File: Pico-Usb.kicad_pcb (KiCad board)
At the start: 2 copper layers, 25 x 60 mm, 40 parts, among them J1 USB_A, J3 MEM2067-02-180-00-A_REVB, J4 10133475-10001LF, SW4 A6H-4101, U1 RP2040, U2 W25Q128JVS, U3 MAX40200AUK, U4 MAX40200AUK, U5 AP2112K-3.3, U6 TS3USB221ARSER, Y2 ABM3B-12.000MHZ-10-1-U-T

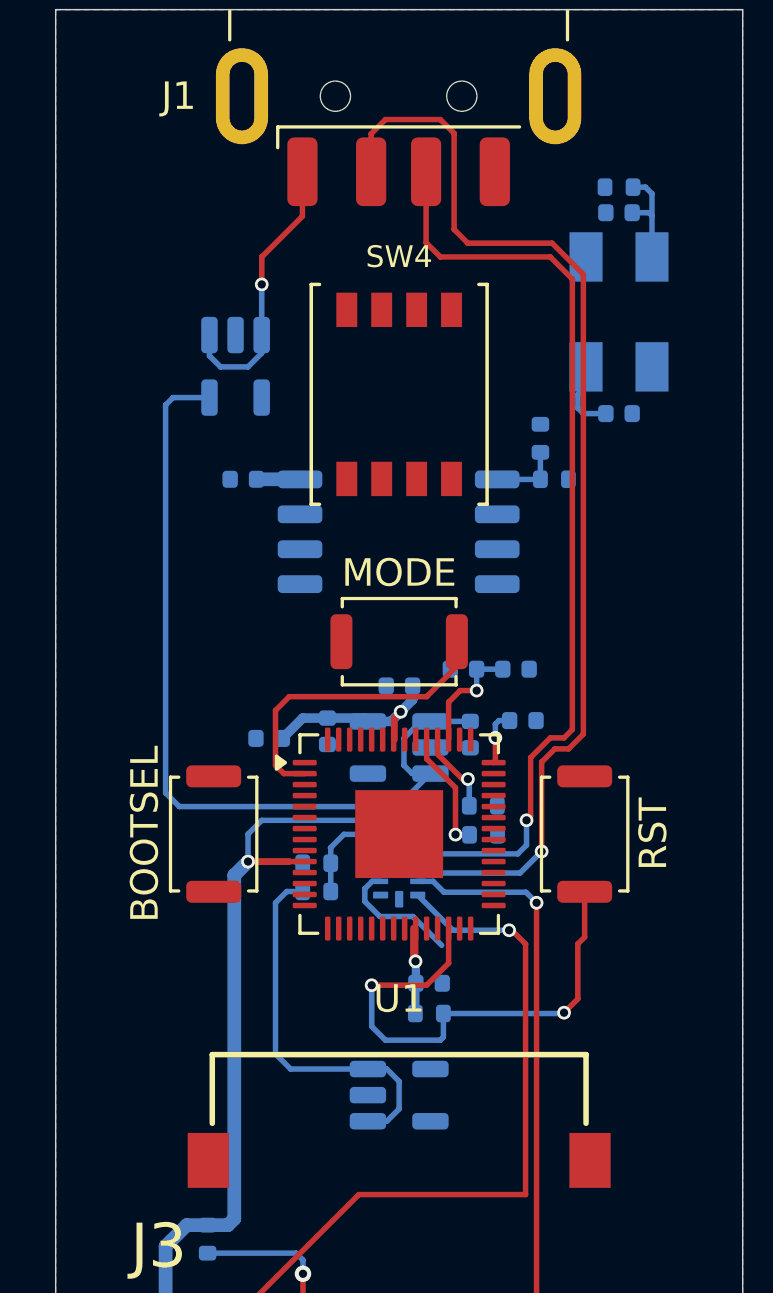
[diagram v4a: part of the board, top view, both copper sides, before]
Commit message: Cambie dimensiones de pistas
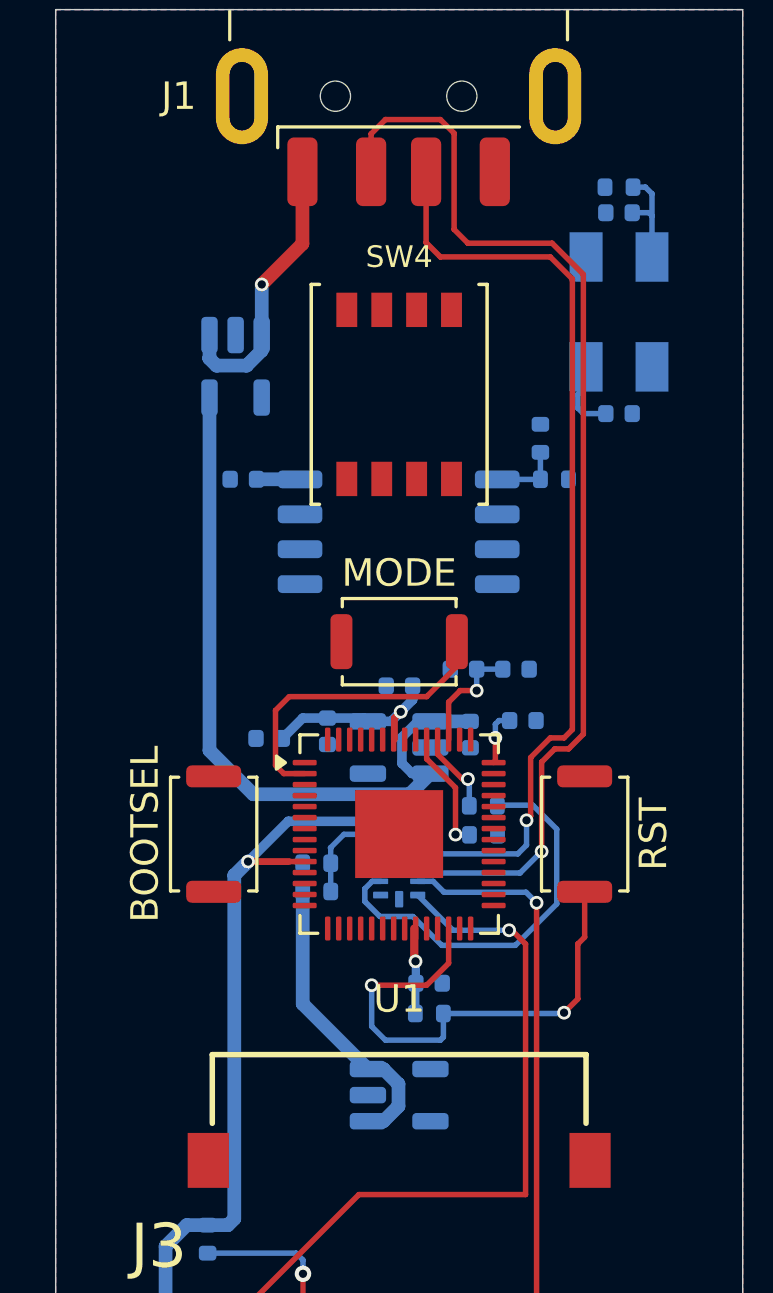
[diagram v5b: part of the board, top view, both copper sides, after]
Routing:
- net /MCU_D-: track 4.61 -> 14.7 mm
- net /5V_Secure: track 30.9 -> 26.7 mm
- net VBUS_A: track 13.9 -> 10.9 mm
- net /3.3V: track 58.0 -> 57.2 mm
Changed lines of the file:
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@@
+	)
+	(segment
+		(start 136.765379 99.535379)
+		(end 133.464621 99.535379)
+		(width 0.35)
+		(layer "B.Cu")
+		(net "/3.3V")
 	)
 	(segment
@@
 		(end 137.20652 95.9)
 		(width 0.35)
-		(layer "B.Cu")
-		(net "/3.3V")
-	)
-	(segment
-		(start 137 99.5)
-		(end 132.5 99.5)
-		(width 0.2)
 		(layer "B.Cu")
 		(net "/3.3V")
@@
 	)
 	(segment
-		(start 137.5 100)
-		(end 137 99.5)
-		(width 0.2)
-		(layer "B.Cu")
-		(net "/3.3V")
-	)
-	(segment
 		(start 142.57 116.99)
 		(end 141.705444 116.99)
@@
 	)
 	(segment
-		(start 137.5 100.57)
-		(end 137.5 100)
-		(width 0.2)
-		(layer "B.Cu")
-		(net "/3.3V")
-	)
-	(segment
 		(start 129.77 114.23)
 		(end 130.53 114.23)
@@
 	)
 	(segment
+		(start 137.5 100.27)
+		(end 136.765379 99.535379)
+		(width 0.35)
+		(layer "B.Cu")
+		(net "/3.3V")
+	)
+	(segment
 		(start 131.8 117.19)
 		(end 129.19 117.19)
 		(width 0.5)
-		(layer "B.Cu")
-		(net "/3.3V")
-	)
-	(segment
-		(start 132.5 99.5)
-		(end 132 100)
-		(width 0.2)
 		(layer "B.Cu")
 		(net "/3.3V")
@@
 	)
 	(segment
-		(start 132 100)
-		(end 132 101)
-		(width 0.2)
-		(layer "B.Cu")
-		(net "/3.3V")
-	)
-	(segment
 		(start 131.5 114)
 		(end 131.5 101.5)
 		(width 0.5)
+		(layer "B.Cu")
+		(net "/3.3V")
+	)
+	(segment
+		(start 133.464621 99.535379)
+		(end 132 101)
+		(width 0.35)
+		(layer "B.Cu")
+		(net "/3.3V")
+	)
+	(segment
+		(start 137.5 100.57)
+		(end 137.5 100.27)
+		(width 0.35)
 		(layer "B.Cu")
 		(net "/3.3V")
@@
 	)
 	(segment
-		(start 132.5 80)
-		(end 132.5 79)
-		(width 0.2)
+		(start 133.98 75.9)
+		(end 133.98 78.52)
+		(width 0.5)
 		(layer "F.Cu")
 		(net "Net-(J1-VBUS)")
 	)
 	(segment
-		(start 132.5 79)
-		(end 133.98 77.52)
-		(width 0.2)
-		(layer "F.Cu")
-		(net "Net-(J1-VBUS)")
-	)
-	(segment
-		(start 133.98 77.52)
-		(end 133.98 75.9)
-		(width 0.2)
+		(start 133.98 78.52)
+		(end 132.5 80)
+		(width 0.5)
 		(layer "F.Cu")
 		(net "Net-(J1-VBUS)")
@@
 	(segment
 		(start 130.5975 81.8425)
-		(end 130.5975 82.5975)
-		(width 0.2)
+		(end 130.5975 82.6825)
+		(width 0.5)
 		(layer "B.Cu")
 		(net "Net-(J1-VBUS)")
 	)
 	(segment
-		(start 130.5975 82.5975)
-		(end 131 83)
-		(width 0.2)
+		(start 130.855 82.955)
+		(end 131.950184 82.955)
+		(width 0.5)
+		(layer "B.Cu")
+		(net "Net-(J1-VBUS)")
+	)
+	(segment
+		(start 132.5 81.84)
+		(end 132.4975 81.8425)
+		(width 0.5)
+		(layer "B.Cu")
+		(net "Net-(J1-VBUS)")
+	)
+	(segment
+		(start 130.59 82.69)
+		(end 130.855 82.955)
+		(width 0.5)
+		(layer "B.Cu")
+		(net "Net-(J1-VBUS)")
+	)
+	(segment
+		(start 130.5975 82.6825)
+		(end 130.59 82.69)
+		(width 0.5)
 		(layer "B.Cu")
 		(net "Net-(J1-VBUS)")
@@
 	)
 	(segment
-		(start 132.4975 82.5025)
+		(start 132.5 80)
+		(end 132.5 81.84)
+		(width 0.5)
+		(layer "B.Cu")
+		(net "Net-(J1-VBUS)")
+	)
+	(segment
+		(start 132.4975 82.407684)
 		(end 132.4975 81.8425)
-		(width 0.2)
+		(width 0.5)
 		(layer "B.Cu")
 		(net "Net-(J1-VBUS)")
 	)
 	(segment
-		(start 132 83)
-		(end 132.4975 82.5025)
-		(width 0.2)
-		(layer "B.Cu")
-		(net "Net-(J1-VBUS)")
-	)
-	(segment
-		(start 132.4975 81.8425)
-		(end 132.4975 80.0025)
-		(width 0.2)
-		(layer "B.Cu")
-		(net "Net-(J1-VBUS)")
-	)
-	(segment
-		(start 131 83)
-		(end 132 83)
-		(width 0.2)
+		(start 131.950184 82.955)
+		(end 132.4975 82.407684)
+		(width 0.5)
 		(layer "B.Cu")
 		(net "Net-(J1-VBUS)")
@@
 	)
 	(segment
-		(start 133 108)
-		(end 133 102.5)
-		(width 0.2)
+		(start 136.927684 110.45)
+		(end 136.3625 110.45)
+		(width 0.5)
 		(layer "B.Cu")
 		(net "VBUS_A")
 	)
 	(segment
-		(start 137.05 108.55)
+		(start 133.99 106.1775)
 		(end 136.3625 108.55)
-		(width 0.2)
+		(width 0.5)
 		(layer "B.Cu")
 		(net "VBUS_A")
 	)
 	(segment
-		(start 137.5 110)
-		(end 137.5 109)
-		(width 0.2)
+		(start 136.927684 108.55)
+		(end 137.475 109.097316)
+		(width 0.5)
 		(layer "B.Cu")
 		(net "VBUS_A")
 	)
 	(segment
-		(start 137.05 110.45)
-		(end 137.5 110)
-		(width 0.2)
+		(start 136.3625 108.55)
+		(end 136.927684 108.55)
+		(width 0.5)
 		(layer "B.Cu")
 		(net "VBUS_A")
 	)
 	(segment
-		(start 133.410001 102.089999)
-		(end 133.99 102.089999)
-		(width 0.2)
+		(start 137.475 109.097316)
+		(end 137.475 109.902684)
+		(width 0.5)
 		(layer "B.Cu")
 		(net "VBUS_A")
 	)
 	(segment
-		(start 136.3625 110.45)
-		(end 137.05 110.45)
-		(width 0.2)
+		(start 137.475 109.902684)
+		(end 136.927684 110.45)
+		(width 0.5)
 		(layer "B.Cu")
 		(net "VBUS_A")
 	)
 	(segment
-		(start 133 102.5)
-		(end 133.410001 102.089999)
-		(width 0.2)
-		(layer "B.Cu")
-		(net "VBUS_A")
-	)
-	(segment
-		(start 133.55 108.55)
-		(end 133 108)
-		(width 0.2)
-		(layer "B.Cu")
-		(net "VBUS_A")
-	)
-	(segment
-		(start 137.5 109)
-		(end 137.05 108.55)
-		(width 0.2)
-		(layer "B.Cu")
-		(net "VBUS_A")
-	)
-	(segment
-		(start 136.3625 108.55)
-		(end 133.55 108.55)
-		(width 0.2)
+		(start 133.99 102.089999)
+		(end 133.99 106.1775)
+		(width 0.5)
 		(layer "B.Cu")
 		(net "VBUS_A")
@@
 	)
 	(segment
-		(start 129 84.389374)
-		(end 129 98.5)
-		(width 0.2)
+		(start 137.8875 98.55)
+		(end 138.6375 97.8)
+		(width 0.5)
+		(layer "B.Cu")
+		(net "/5V_Secure")
+	)
+	(segment
+		(start 137.6 96.478382)
+		(end 137.6 97.424999)
+		(width 0.35)
+		(layer "B.Cu")
+		(net "/5V_Secure")
+	)
+	(segment
+		(start 138.6375 95.9)
+		(end 138.178382 95.9)
+		(width 0.35)
+		(layer "B.Cu")
+		(net "/5V_Secure")
+	)
+	(segment
+		(start 138.178382 95.9)
+		(end 137.6 96.478382)
+		(width 0.35)
+		(layer "B.Cu")
+		(net "/5V_Secure")
+	)
+	(segment
+		(start 137.6 97.424999)
+		(end 137.975001 97.8)
+		(width 0.35)
 		(layer "B.Cu")
 		(net "/5V_Secure")
@@
 		(start 137.975001 97.8)
 		(end 138.6375 97.8)
-		(width 0.2)
-		(layer "B.Cu")
-		(net "/5V_Secure")
-	)
-	(segment
-		(start 129.271874 84.1175)
-		(end 129 84.389374)
-		(width 0.2)
-		(layer "B.Cu")
-		(net "/5V_Secure")
-	)
-	(segment
-		(start 137.4375 99)
-		(end 138.6375 97.8)
-		(width 0.2)
-		(layer "B.Cu")
-		(net "/5V_Secure")
-	)
-	(segment
-		(start 129.5 99)
-		(end 137.4375 99)
-		(width 0.2)
-		(layer "B.Cu")
-		(net "/5V_Secure")
-	)
-	(segment
-		(start 129 98.5)
-		(end 129.5 99)
-		(width 0.2)
-		(layer "B.Cu")
-		(net "/5V_Secure")
-	)
-	(segment
-		(start 137.675 96.509448)
-		(end 137.675 97.499999)
-		(width 0.2)
-		(layer "B.Cu")
-		(net "/5V_Secure")
-	)
-	(segment
-		(start 137.675 97.499999)
-		(end 137.975001 97.8)
-		(width 0.2)
-		(layer "B.Cu")
-		(net "/5V_Secure")
-	)
-	(segment
-		(start 138.6375 95.9)
-		(end 138.284448 95.9)
-		(width 0.2)
+		(width 0.35)
 		(layer "B.Cu")
 		(net "/5V_Secure")
@@
 		(start 138.6375 95.9)
 		(end 140.09 95.9)
-		(width 0.2)
+		(width 0.5)
 		(layer "B.Cu")
 		(net "/5V_Secure")
 	)
 	(segment
-		(start 138.284448 95.9)
-		(end 137.675 96.509448)
-		(width 0.2)
+		(start 130.5975 84.1175)
+		(end 130.5975 96.9575)
+		(width 0.5)
 		(layer "B.Cu")
 		(net "/5V_Secure")
 	)
 	(segment
-		(start 130.5975 84.1175)
-		(end 129.271874 84.1175)
-		(width 0.2)
+		(start 130.5975 96.9575)
+		(end 132.19 98.55)
+		(width 0.5)
+		(layer "B.Cu")
+		(net "/5V_Secure")
+	)
+	(segment
+		(start 132.19 98.55)
+		(end 137.8875 98.55)
+		(width 0.5)
 		(layer "B.Cu")
 		(net "/5V_Secure")
@@
 	)
 	(segment
+		(start 139.05 104.05)
+		(end 141.727818 104.05)
+		(width 0.2)
+		(layer "B.Cu")
+		(net "/MCU_D-")
+	)
+	(segment
+		(start 143.234204 99.822182)
+		(end 142.362022 98.95)
+		(width 0.2)
+		(layer "B.Cu")
+		(net "/MCU_D-")
+	)
+	(segment
+		(start 141.727818 104.05)
+		(end 143.234204 102.543614)
+		(width 0.2)
+		(layer "B.Cu")
+		(net "/MCU_D-")
+	)
+	(segment
+		(start 141.094667 98.95)
+		(end 141.071735 98.972932)
+		(width 0.2)
+		(layer "B.Cu")
+		(net "/MCU_D-")
+	)
+	(segment
 		(start 136.518176 101.72)
 		(end 136.25 101.988176)
 		(width 0.2)
 		(layer "B.Cu")
+		(net "/MCU_D-")
+	)
+	(segment
+		(start 143.234204 102.543614)
+		(end 143.234204 99.822182)
+		(width 0.2)
+		(layer "B.Cu")
+		(net "/MCU_D-")
+	)
+	(segment
+		(start 142.362022 98.95)
+		(end 141.094667 98.95)
+		(width 0.2)
+		(layer "B.Cu")

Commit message: reconfigure pistas para liberar componentes
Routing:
- net VBUS_A: track 10.9 -> 50.8 mm, vias 0 -> 2
- net Net-(U1-GPIO0): track 11.3 -> 31.5 mm, vias 0 -> 2
- net /MCU_D+: track 0.00 -> 20.0 mm, vias 0 -> 2
- net /3.3V: track 57.2 -> 68.4 mm
- net /QSPI_SS: track 2.55 -> 10.7 mm, vias 0 -> 1
- net /USB_C_D-: track 39.3 -> 44.5 mm, vias 1 -> 2
- net /USB_A_D+: track 34.1 -> 38.4 mm
- net /USB_A_D-: track 40.5 -> 44.6 mm
- net /MCU_D-: track 14.7 -> 16.9 mm
- net /USB_C_D+: track 34.4 -> 36.5 mm, vias 1 -> 2

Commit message: complete el ruteo de la memoria al rp2040
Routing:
- net Net-(U1-XOUT): track 0.00 -> 47.7 mm, vias 0 -> 1
- net Net-(U1-XIN): track 2.73 -> 44.1 mm, vias 0 -> 1
- net Net-(R5-Pad1): track 0.00 -> 25.6 mm, vias 0 -> 5
- net /SPI_RX: track 6.00 -> 26.9 mm, vias 1 -> 2
- net /SPI_CS: track 0.00 -> 15.8 mm, vias 0 -> 2
- net /QSPI_SCLK: track 0.00 -> 13.2 mm, vias 0 -> 3
- net /QSPI_SD3: track 0.00 -> 12.5 mm, vias 0 -> 3
- net /QSPI_SD0: track 0.00 -> 12.5 mm, vias 0 -> 1
- net /QSPI_SD1: track 0.00 -> 12.1 mm, vias 0 -> 1
- net /QSPI_SD2: track 0.00 -> 10.9 mm, vias 0 -> 1
- net VBUS_A: track 50.8 -> 60.3 mm
- net /QSPI_SS: track 10.7 -> 19.5 mm
- net GNDREF: track 0.00 -> 7.23 mm
- net /3.3V: track 68.4 -> 71.5 mm, vias 5 -> 6
- net Net-(U1-RUN): track 18.7 -> 18.2 mm

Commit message: Termine el ruteo
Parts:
- renumbered SW4 to CFG
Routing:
- net /SWD-1: track 0.00 -> 39.0 mm, vias 0 -> 2
- net /SWD-2: track 0.00 -> 38.6 mm, vias 0 -> 2
- net /SWD-3: track 0.00 -> 38.5 mm, vias 0 -> 2
- net /SWD-4: track 0.00 -> 38.0 mm, vias 0 -> 2
- net /SPI_SCK: track 0.00 -> 25.3 mm, vias 0 -> 4
- net /SPI_TX: track 0.00 -> 25.1 mm, vias 0 -> 2
- net /USB_C_D+: track 36.5 -> 37.8 mm
- net /MCU_D+: track 20.0 -> 21.1 mm
- net /MCU_D-: track 16.9 -> 17.5 mm
- net /USB_C_D-: track 44.5 -> 43.9 mm
